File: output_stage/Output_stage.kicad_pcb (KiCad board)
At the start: 2 copper layers, 62.9 x 27.9 mm, 16 parts, among them J1 Conn_01x03_Socket, J2 Control/LED, J3 Control/LED, Q1 BTA41, U1 MOC30x1

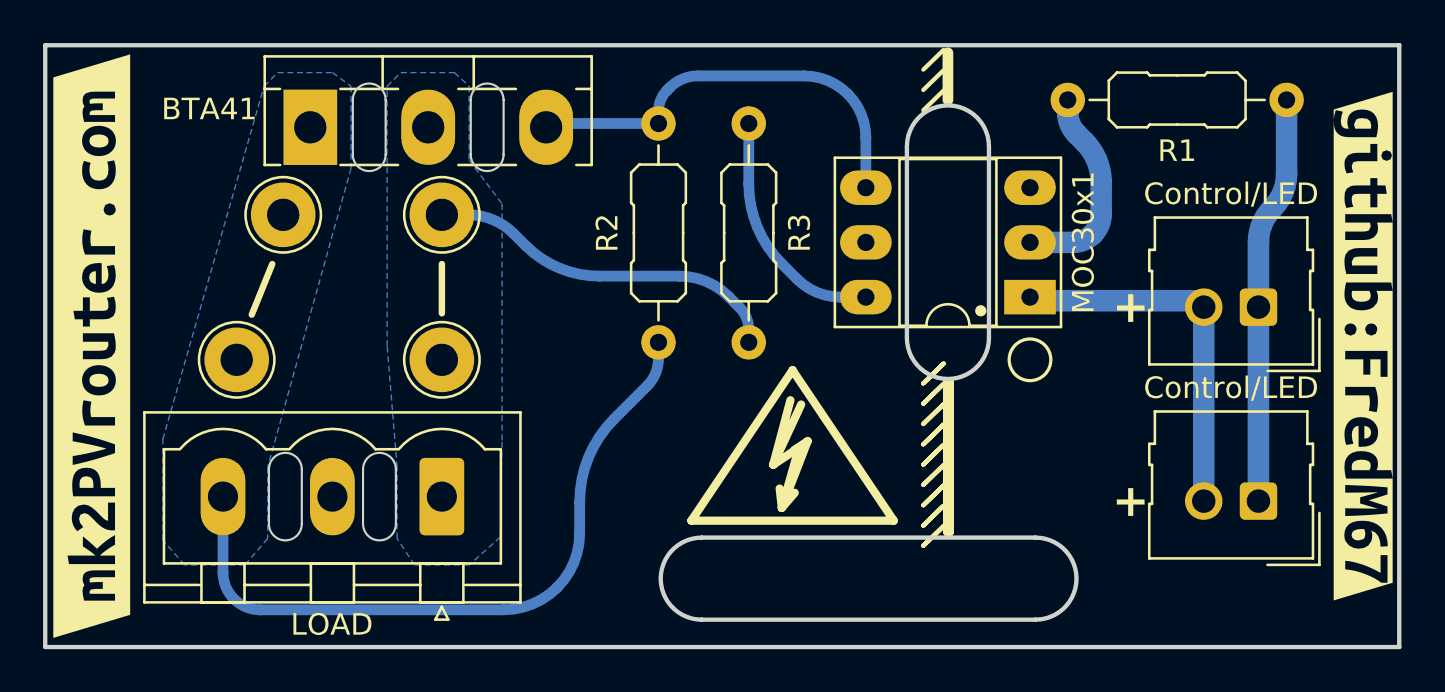
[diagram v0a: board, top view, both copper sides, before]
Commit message: Add gitignore entries for DRC/BOM/simulation temp files
Also includes output_stage project files updated by KiCad 9.

Co-Authored-By: Claude Opus 4.6 <noreply@anthropic.com>
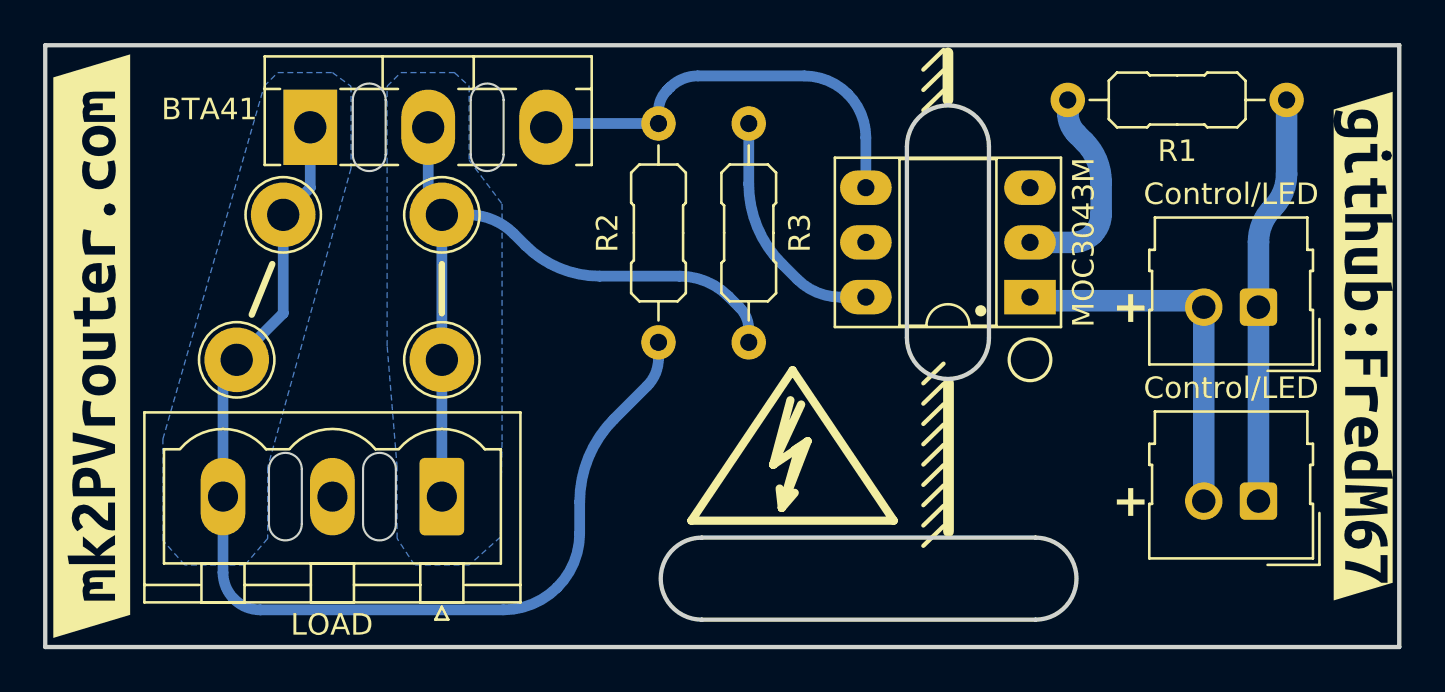
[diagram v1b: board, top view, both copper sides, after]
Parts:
- R1: value 120 -> 220
- U1: value MOC30x1 -> MOC3043M
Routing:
- net S/LINE: track 35.3 -> 54.1 mm
- net LINE: track 16.8 -> 34.2 mm
